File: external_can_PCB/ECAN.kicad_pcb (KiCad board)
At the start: 4 copper layers, 42.8 x 38.1 mm, 13 parts, among them J1 Conn_01x04, J2 Conn_01x06, J4 Conn_02x05_Top_Bottom, U2 SN65HVD230, U3 TXB0104D, U4 IFX27001TFV33, U5 STM32L562RETx

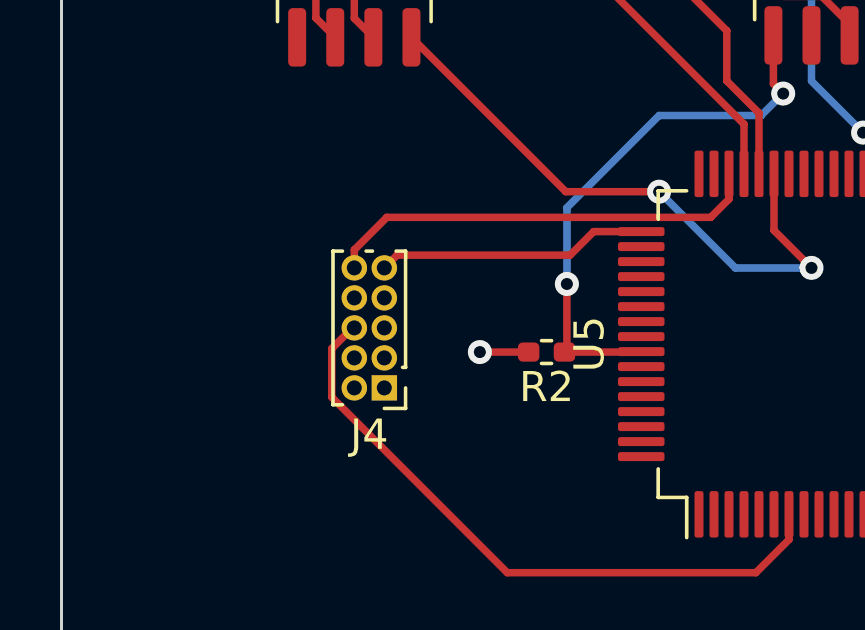
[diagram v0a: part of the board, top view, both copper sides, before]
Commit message: Added micro SD Card slot and oscillator
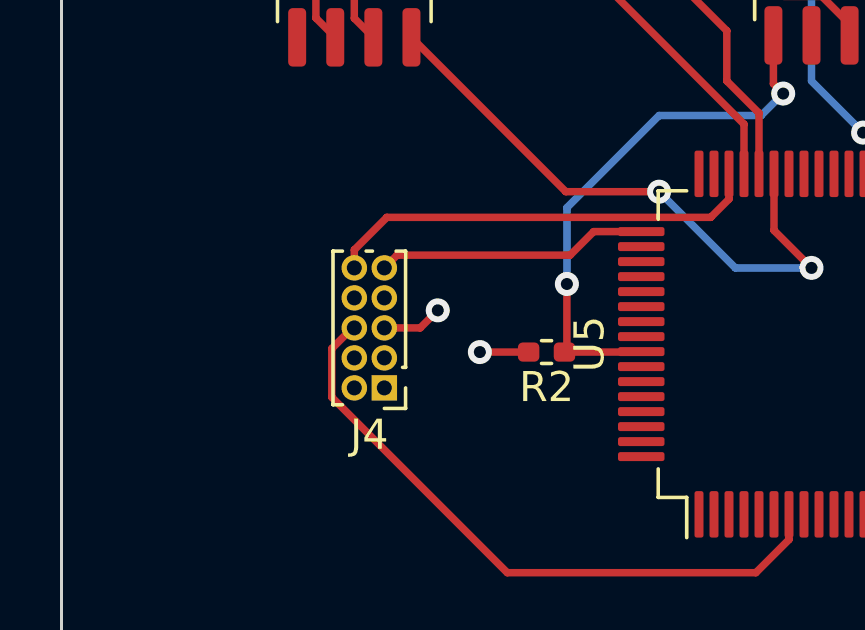
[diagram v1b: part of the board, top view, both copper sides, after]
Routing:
- net GND: track 22.5 -> 24.5 mm, vias 8 -> 9
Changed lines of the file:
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@@
   (segment (start 157.933364 78.74) (end 159.459682 80.266318) (width 0.25) (layer "F.Cu") (net 2))
   (segment (start 151.07 74.87) (end 149.86 73.66) (width 0.25) (layer "F.Cu") (net 2))
+  (segment (start 129.19754 95.98) (end 129.782471 95.395069) (width 0.25) (layer "F.Cu") (net 2))
   (segment (start 140.97 79.687518) (end 141.382865 79.274653) (width 0.25) (layer "F.Cu") (net 2))
   (segment (start 130.75 78.8024) (end 130.77949 78.83189) (width 0.25) (layer "F.Cu") (net 2))
@@
   (segment (start 153.745728 79.13812) (end 157.08188 79.13812) (width 0.25) (layer "F.Cu") (net 2))
   (segment (start 132.811255 96.785413) (end 131.185457 96.785413) (width 0.25) (layer "F.Cu") (net 2))
+  (segment (start 128 95.98) (end 129.19754 95.98) (width 0.25) (layer "F.Cu") (net 2))
   (segment (start 151.07 76.1925) (end 151.07 74.87) (width 0.25) (layer "F.Cu") (net 2))
   (segment (start 149.86 80.7125) (end 149.86 78.74) (width 0.25) (layer "F.Cu") (net 2))
@@
   (via (at 149.86 83.82) (size 0.8) (drill 0.4) (layers "F.Cu" "B.Cu") (net 2))
   (via (at 131.185457 96.785413) (size 0.8) (drill 0.4) (layers "F.Cu" "B.Cu") (net 2))
+  (via (at 129.782471 95.395069) (size 0.8) (drill 0.4) (layers "F.Cu" "B.Cu") (net 2))
   (via (at 149.86 78.74) (size 0.8) (drill 0.4) (layers "F.Cu" "B.Cu") (net 2))
   (segment (start 159.459682 81.401318) (end 158.156 82.705) (width 0.25) (layer "F.Cu") (net 3))

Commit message: PCB layout v1
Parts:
- removed J2: Conn_01x06, Connector_JST:JST_EH_S6B-EH_1x06_P2.50mm_Horizontal
- removed U4: IFX27001TFV33, Package_TO_SOT_SMD:TO-252-3_TabPin2
- added C10: 0.1 uF, Capacitor_SMD:C_0402_1005Metric_Pad0.74x0.62mm_HandSolder, B.Cu at (128.5, 75.2)
- added C11: 0.1 uF, Capacitor_SMD:C_0402_1005Metric_Pad0.74x0.62mm_HandSolder, F.Cu at (154.5, 59.3)
- added C12: 0.1 uF, Capacitor_SMD:C_0402_1005Metric_Pad0.74x0.62mm_HandSolder, F.Cu at (143.1, 75.4)
- added C13: 0.1 uF, Capacitor_SMD:C_0402_1005Metric_Pad0.74x0.62mm_HandSolder, F.Cu at (153.4, 65.5)
- added C14: 0.1 uF, Capacitor_SMD:C_0402_1005Metric_Pad0.74x0.62mm_HandSolder, F.Cu at (153.4, 61.0)
- added C15: 0.1 uF, Capacitor_SMD:C_0402_1005Metric_Pad0.74x0.62mm_HandSolder, F.Cu at (140.5, 63.3)
- added C16: 0.1 uF, Capacitor_SMD:C_0402_1005Metric_Pad0.74x0.62mm_HandSolder, F.Cu at (140.0, 48.7)
- added C17: 0.1 uF, Capacitor_SMD:C_0402_1005Metric_Pad0.74x0.62mm_HandSolder, F.Cu at (133.5, 48.7)
- added C5: 5pF, Capacitor_SMD:C_0402_1005Metric_Pad0.74x0.62mm_HandSolder, F.Cu at (126.2, 63.8)
- added C6: 5pF, Capacitor_SMD:C_0402_1005Metric_Pad0.74x0.62mm_HandSolder, F.Cu at (126.2, 52.6)
- added C7: 100nF, Capacitor_SMD:C_0402_1005Metric_Pad0.74x0.62mm_HandSolder, F.Cu at (144.2, 59.1)
- added C8: 0.1 uF, Capacitor_SMD:C_0402_1005Metric_Pad0.74x0.62mm_HandSolder, F.Cu at (148.1, 60.0)
- added C9: 0.1 uF, Capacitor_SMD:C_0402_1005Metric_Pad0.74x0.62mm_HandSolder, F.Cu at (131.6, 61.8)
- added D1: SM712_SOT23, Package_TO_SOT_SMD:SOT-23, F.Cu at (153.0, 63.3)
- added J3: JST SH 6, Connector_JST:JST_SH_BM06B-SRSS-TB_1x06-1MP_P1.00mm_Vertical, F.Cu at (137.4, 77.2)
- added J5: JST SH 6, Connector_JST:JST_SH_BM06B-SRSS-TB_1x06-1MP_P1.00mm_Vertical, F.Cu at (157.7, 52.7)
- added R3: 100k, Resistor_SMD:R_0402_1005Metric_Pad0.72x0.64mm_HandSolder, B.Cu at (140.1, 65.0)
- added R4: 100k, Resistor_SMD:R_0402_1005Metric_Pad0.72x0.64mm_HandSolder, B.Cu at (142.4, 65.0)
- added R5: 100k, Resistor_SMD:R_0402_1005Metric_Pad0.72x0.64mm_HandSolder, B.Cu at (133.5, 65.0)
- added R6: 100k, Resistor_SMD:R_0402_1005Metric_Pad0.72x0.64mm_HandSolder, B.Cu at (135.8, 65.0)
- added R7: 200k, Resistor_SMD:R_0402_1005Metric_Pad0.72x0.64mm_HandSolder, F.Cu at (128.3, 55.8)
- added R8: 100k, Resistor_SMD:R_0402_1005Metric_Pad0.72x0.64mm_HandSolder, F.Cu at (134.3, 73.9)
- added R9: 100k, Resistor_SMD:R_0402_1005Metric_Pad0.72x0.64mm_HandSolder, F.Cu at (135.3, 72.4)
- added U1: SN65HVD232, Package_SO:SOIC-8_3.9x4.9mm_P1.27mm, F.Cu at (146.6, 63.3)
- added Y1: 8 Mhz, Crystal:Crystal_SMD_0603-2Pin_6.0x3.5mm_HandSoldering, F.Cu at (125.7, 58.2)
- C1: value 100 nF -> 1 uF
- C2: value 10 uF -> 1 uF
- J1: value Conn_01x04 -> JST SH 4; footprint Connector_JST:JST_EH_S4B-EH_1x04_P2.50mm_Horizontal -> Connector_JST:JST_SH_BM04B-SRSS-TB_1x04-1MP_P1.00mm_Vertical
- J4: value Conn_02x05_Top_Bottom -> Micro_SD_Card; footprint Connector_PinHeader_1.00mm:PinHeader_2x05_P1.00mm_Vertical -> Connector_Card:microSD_HC_Wuerth_693072010801; moved to B.Cu
- U2: value SN65HVD230 -> AP2127N-3.3; footprint Package_SO:SOIC-8_3.9x4.9mm_P1.27mm -> Package_TO_SOT_SMD:SOT-223-3_TabPin2
- moved U2 45.8 mm to (150.0, 44.2), turned to 180 degrees
- moved R2 42.2 mm to (152.1, 58.9)
- moved U5 40.9 mm to (137.0, 56.0), turned to 180 degrees
- moved C2 38.9 mm to (145.0, 44.8), turned to -90 degrees
- moved C3 37.7 mm to (151.9, 48.7), turned to 0 degrees
- moved J1 37.3 mm to (157.8, 62.2), turned to -90 degrees
- moved C4 32.6 mm to (148.6, 48.7), turned to 180 degrees
- moved C1 32.1 mm to (156.8, 47.2)
- moved U3 30.4 mm to (150.1, 53.8), turned to 0 degrees
- moved R1 28.4 mm to (150.7, 63.3), turned to -90 degrees
- moved J4 25.7 mm to (137.3, 74.0), turned to 0 degrees
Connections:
- C1 pad 1: Net-(J2-Pin_6) -> Net-(J5-Pin_1)
- C3 pad 1: Net-(J2-Pin_6) -> Net-(J5-Pin_1)
- J1 pad 2: Net-(J1-Pin_2) -> GND
- J1 pad 3: Net-(J1-Pin_3) -> Net-(D1-A2)
- J1 pad 4: GND -> Net-(D1-A1)
- J4 pad 1: +3.3V -> Net-(J4-DAT2)
- J4 pad 2: unconnected-(J4-Pin_2-Pad2) -> Net-(J4-DAT3/CD)
- J4 pad 3: unconnected-(J4-Pin_3-Pad3) -> Net-(J4-CMD)
- J4 pad 4: unconnected-(J4-Pin_4-Pad4) -> +3.3V
- J4 pad 5: GND -> Net-(J4-CLK)
- J4 pad 6: Net-(J4-Pin_6) -> GND
- J4 pad 7: unconnected-(J4-Pin_7-Pad7) -> Net-(J4-DAT0)
- J4 pad 8: unconnected-(J4-Pin_8-Pad8) -> Net-(J4-DAT1)
- J4 pad 9: Net-(J4-Pin_9) -> GND
- R1 pad 1: Net-(J1-Pin_2) -> Net-(D1-A2)
- R1 pad 2: Net-(J1-Pin_3) -> Net-(D1-A1)
- U2 pad 1: Net-(U2-D) -> GND
- U2 pad 2: GND -> +3.3V
- U2 pad 3: +3.3V -> Net-(J5-Pin_1)
- U3 pad 14: Net-(J2-Pin_6) -> Net-(J5-Pin_1)
- U5 pad 1: unconnected-(U5-VBAT-Pad1) -> Net-(U5-VBAT)
- U5 pad 12: unconnected-(U5-VSSA-Pad12) -> GND
- U5 pad 13: unconnected-(U5-VDDA-Pad13) -> +3V3
- U5 pad 39: unconnected-(U5-PC8-Pad39) -> Net-(J4-DAT0)
- U5 pad 40: unconnected-(U5-PC9-Pad40) -> Net-(J4-DAT1)
- U5 pad 43: Net-(U2-Rs) -> unconnected-(U5-PA10-Pad43)
- U5 pad 44: Net-(U2-R) -> Net-(U1-R)
- U5 pad 45: Net-(U2-D) -> Net-(U1-D)
- U5 pad 46: Net-(J4-Pin_10) -> Net-(J3-Pin_4)
- U5 pad 48: unconnected-(U5-VDDUSB-Pad48) -> +3V3
- U5 pad 49: Net-(J4-Pin_9) -> Net-(J3-Pin_3)
- U5 pad 5: unconnected-(U5-PH0-Pad5) -> Net-(U5-PH0)
- U5 pad 51: unconnected-(U5-PC10-Pad51) -> Net-(J4-DAT2)
- U5 pad 52: unconnected-(U5-PC11-Pad52) -> Net-(J4-DAT3/CD)
- U5 pad 53: unconnected-(U5-PC12-Pad53) -> Net-(J4-CLK)
- U5 pad 54: unconnected-(U5-PD2-Pad54) -> Net-(J4-CMD)
- U5 pad 6: unconnected-(U5-PH1-Pad6) -> Net-(U5-PH1)
- U5 pad 60: unconnected-(U5-PH3-Pad60) -> Net-(J3-Pin_5)
- U5 pad 7: Net-(J4-Pin_6) -> Net-(J3-Pin_6)
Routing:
- net Net-(J3-Pin_6): track 0.00 -> 28.5 mm
- net Net-(J4-DAT1): track 0.00 -> 27.2 mm, vias 0 -> 1
- net Net-(U2-R): track 26.9 -> 0.00 mm, vias 2 -> 0
- net Net-(J4-DAT0): track 0.00 -> 26.5 mm, vias 0 -> 1
- net Net-(J4-Pin_6): track 21.6 -> 0.00 mm
- net Net-(J3-Pin_4): track 0.00 -> 21.3 mm, vias 0 -> 2
- net Net-(U5-PH0): track 0.00 -> 21.0 mm, vias 0 -> 2
- net Net-(U1-D): track 0.00 -> 20.6 mm, vias 0 -> 2
- net Net-(U2-Rs): track 20.2 -> 0.00 mm, vias 2 -> 0
- net Net-(J2-Pin_6): track 19.9 -> 0.00 mm
- net Net-(U1-R): track 0.00 -> 19.7 mm, vias 0 -> 2
- net GND: track 24.5 -> 44.0 mm, vias 9 -> 24
- net +3.3V: track 18.4 -> 36.0 mm, vias 2 -> 5
- net Net-(J3-Pin_3): track 0.00 -> 16.8 mm, vias 0 -> 2
- net Net-(U2-D): track 16.0 -> 0.00 mm
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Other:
- board outline removed

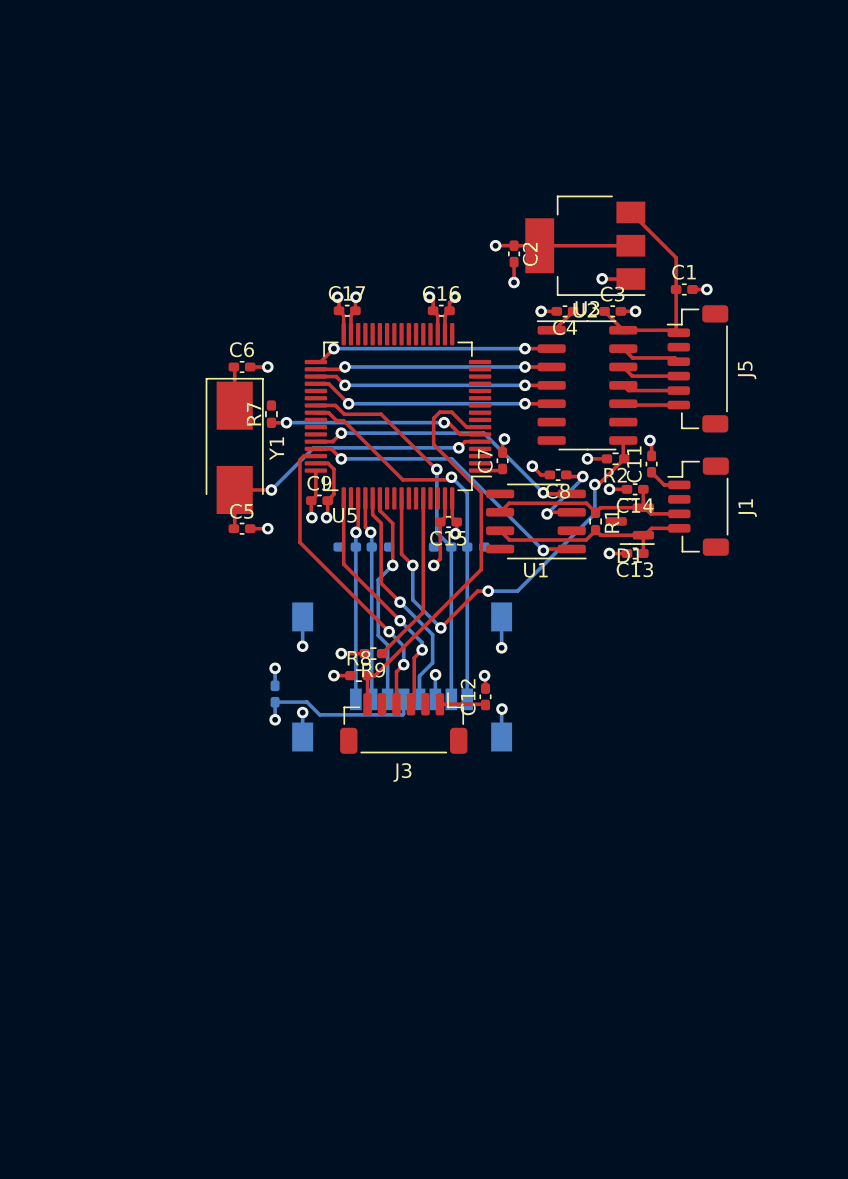
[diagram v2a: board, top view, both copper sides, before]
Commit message: Redid ECAN Design: - Removed SPI Level Shifter * Changed JST SH Connector to JST GH * Cleaned up schematic
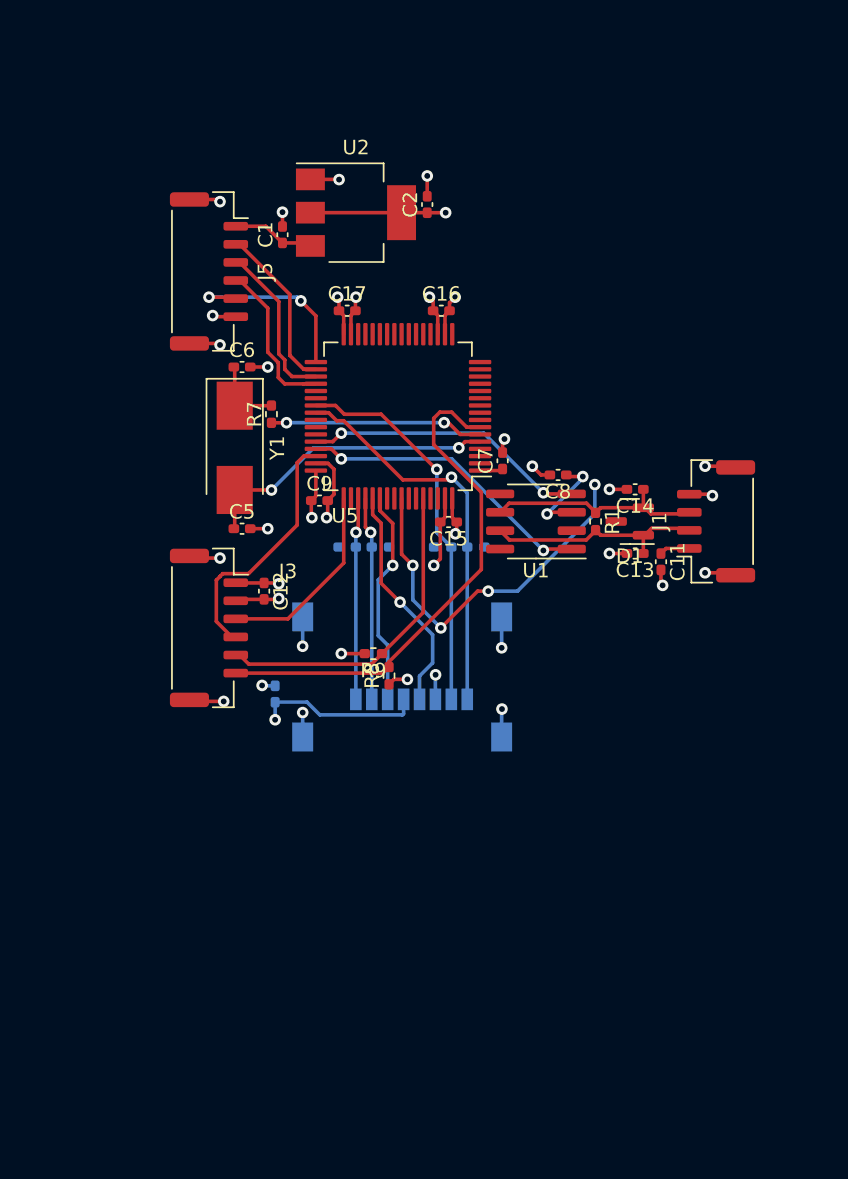
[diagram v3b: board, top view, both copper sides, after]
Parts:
- removed C3, C4: 0.1 uF, Capacitor_SMD:C_0402_1005Metric_Pad0.74x0.62mm_HandSolder
- removed R2: 55 kOhm, Resistor_SMD:R_0402_1005Metric_Pad0.72x0.64mm_HandSolder
- removed U3: TXB0104D, Package_SO:SOIC-14_3.9x8.7mm_P1.27mm
- J1: value JST SH 4 -> JST GH 4; footprint Connector_JST:JST_SH_BM04B-SRSS-TB_1x04-1MP_P1.00mm_Vertical -> Connector_JST:JST_GH_SM04B-GHS-TB_1x04-1MP_P1.25mm_Horizontal
- J3, J5: value JST SH 6 -> JST GH 6; footprint Connector_JST:JST_SH_BM06B-SRSS-TB_1x06-1MP_P1.00mm_Vertical -> Connector_JST:JST_GH_SM06B-GHS-TB_1x06-1MP_P1.25mm_Horizontal
- moved J5 34.5 mm to (124.0, 46.0)
- moved C1 28.0 mm to (129.0, 43.4), turned to 90 degrees
- moved C12 17.0 mm to (127.8, 68.1), turned to -90 degrees
- moved U2 16.0 mm to (134.1, 41.9), turned to 0 degrees
- moved J3 15.0 mm to (124.0, 70.6), turned to -90 degrees
- moved C2 6.90 mm to (139.0, 41.3), turned to 90 degrees
- moved C11 6.78 mm to (155.2, 66.0), turned to -90 degrees
- moved R8 2.08 mm to (136.4, 73.9), turned to 90 degrees
- moved J1 1.59 mm to (159.0, 63.2), turned to 90 degrees
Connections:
- net Net-(J3-Pin_3) renamed /JTCK/SWCLK
- net Net-(J3-Pin_4) renamed /JTMS/SWDIO
- net Net-(J3-Pin_5) renamed /BOOT0
- net Net-(J3-Pin_6) renamed /NRST
- net Net-(U1-D) renamed /FDCAN1_TX
- net Net-(U1-R) renamed /FDCAN1_RX
- C15 pad 1: +3V3 -> +3.3V
- C16 pad 1: +3V3 -> +3.3V
- C17 pad 1: +3V3 -> +3.3V
- C7 pad 2: +3V3 -> +3.3V
- C9 pad 1: +3V3 -> +3.3V
- J1 pad 2: GND -> Net-(D1-A1)
- J1 pad 4: Net-(D1-A1) -> GND
- J5 pad 2: GND -> /SPI2_SCK_3.3V
- J5 pad 3: Net-(J5-Pin_3) -> /SPI3_MISO_3.3V
- J5 pad 4: Net-(J5-Pin_4) -> /SPI2_MOSI_3.3V
- J5 pad 5: Net-(J5-Pin_5) -> /SPI2_NSS_3.3V
- J5 pad 6: Net-(J5-Pin_6) -> GND
- U5 pad 13: +3V3 -> +3.3V
- U5 pad 19: +3V3 -> +3.3V
- U5 pad 32: +3V3 -> +3.3V
- U5 pad 33: Net-(U3-A1) -> /SPI2_NSS_3.3V
- U5 pad 34: Net-(U3-A2) -> /SPI2_SCK_3.3V
- U5 pad 35: Net-(U3-A3) -> /SPI3_MISO_3.3V
- U5 pad 36: Net-(U3-A4) -> /SPI2_MOSI_3.3V
- U5 pad 48: +3V3 -> +3.3V
- U5 pad 57: Net-(U3-OE) -> unconnected-(U5-PB5-Pad57)
- U5 pad 64: +3V3 -> +3.3V
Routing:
- net Net-(U3-OE): track 30.1 -> 0.00 mm, vias 4 -> 0
- net unconnected-(U5-PB5-Pad57): track 0.00 -> 26.3 mm, vias 0 -> 4
- net Net-(U3-A4): track 16.9 -> 0.00 mm, vias 2 -> 0
- net Net-(U3-A1): track 16.7 -> 0.00 mm, vias 2 -> 0
- net Net-(U3-A3): track 16.6 -> 0.00 mm, vias 2 -> 0
- net Net-(U3-A2): track 16.4 -> 0.00 mm, vias 2 -> 0
- net GND: track 44.0 -> 58.8 mm, vias 24 -> 29
- net /SPI2_NSS_3.3V: track 0.00 -> 13.0 mm, vias 0 -> 2
- net +3V3: track 12.5 -> 0.00 mm, vias 5 -> 0
- net /SPI2_SCK_3.3V: track 0.00 -> 11.6 mm
- net /SPI3_MISO_3.3V: track 0.00 -> 11.3 mm
- net /SPI2_MOSI_3.3V: track 0.00 -> 10.9 mm
- net /BOOT0: track 11.9 -> 22.6 mm
- net +3.3V: track 36.0 -> 46.5 mm, vias 5 -> 11
- net Net-(J5-Pin_1): track 15.4 -> 5.72 mm
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
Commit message: Added screw holes and layer pours
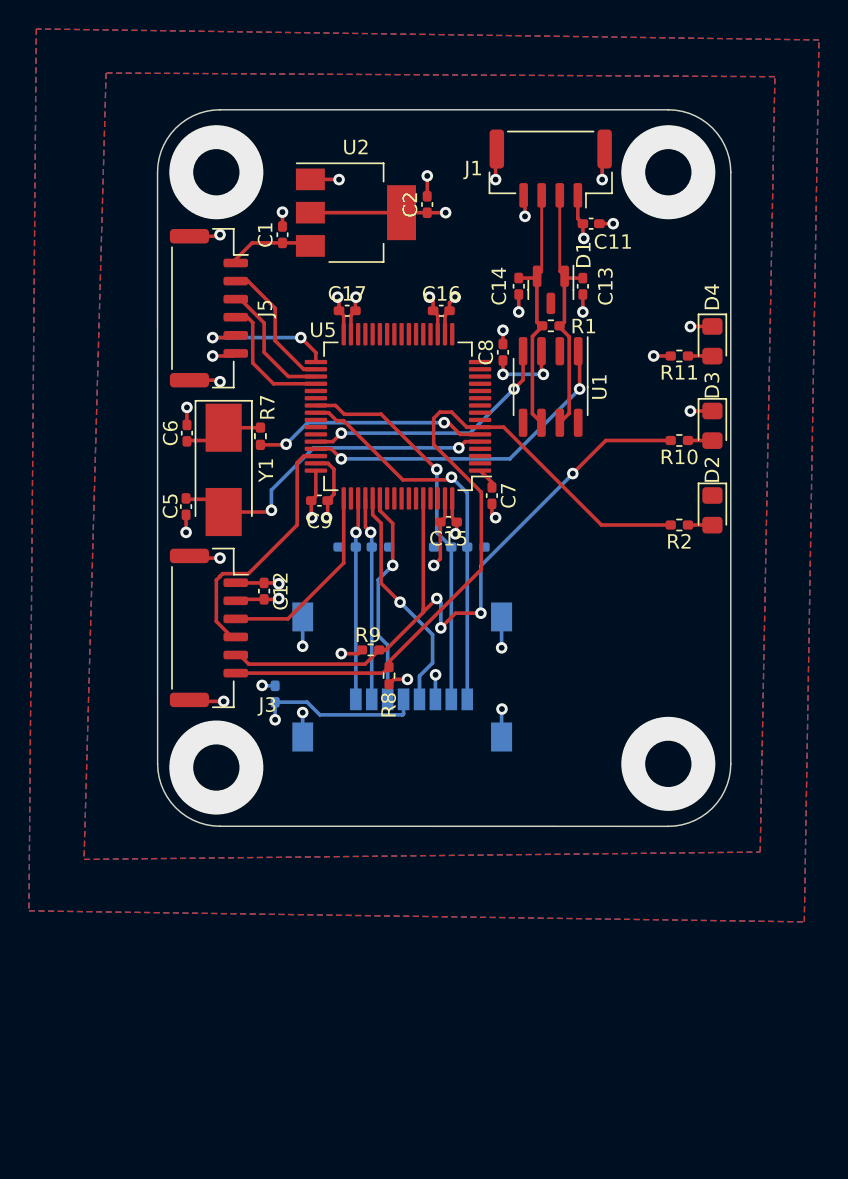
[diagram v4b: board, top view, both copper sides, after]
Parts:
- added D2: LED, LED_SMD:LED_0805_2012Metric_Pad1.15x1.40mm_HandSolder, F.Cu at (158.8, 62.5)
- added D3: LED, LED_SMD:LED_0805_2012Metric_Pad1.15x1.40mm_HandSolder, F.Cu at (158.8, 56.6)
- added D4: LED, LED_SMD:LED_0805_2012Metric_Pad1.15x1.40mm_HandSolder, F.Cu at (158.8, 50.8)
- added R10: 220, Resistor_SMD:R_0402_1005Metric_Pad0.72x0.64mm_HandSolder, F.Cu at (156.5, 57.7)
- added R11: 220, Resistor_SMD:R_0402_1005Metric_Pad0.72x0.64mm_HandSolder, F.Cu at (156.5, 51.8)
- added R2: 200, Resistor_SMD:R_0402_1005Metric_Pad0.72x0.64mm_HandSolder, F.Cu at (156.5, 63.5)
- moved J1 26.9 mm to (147.6, 38.9), turned to 180 degrees
- moved C11 23.9 mm to (150.4, 42.7), turned to 0 degrees
- moved C13 18.8 mm to (149.8, 47.0), turned to -90 degrees
- moved D1 16.9 mm to (147.6, 47.2), turned to -90 degrees
- moved C14 16.2 mm to (145.4, 47.0), turned to -90 degrees
- moved R1 13.9 mm to (147.6, 49.7), turned to 0 degrees
- moved U1 9.35 mm to (147.6, 54.0), turned to -90 degrees
- moved C8 9.29 mm to (144.3, 51.6), turned to 90 degrees
- moved C6 5.95 mm to (122.4, 57.1), turned to 90 degrees
- moved C5 4.16 mm to (122.4, 62.2), turned to -90 degrees
- moved J5 2.54 mm to (124.0, 48.5)
- moved C7 2.52 mm to (143.5, 61.5), turned to -90 degrees
- moved R7 1.70 mm to (127.5, 57.4)
- moved Y1 1.70 mm to (125.0, 59.7)
- moved R9 0.32 mm to (135.1, 72.1)
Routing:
- net /BOOT0: track 22.6 -> 49.3 mm, vias 0 -> 4
- net unconnected-(U5-PB5-Pad57): track 26.3 -> 0.00 mm, vias 4 -> 0
- net /NRST: track 35.6 -> 51.6 mm
- net Net-(D1-A2): track 14.5 -> 17.7 mm
- net Net-(D1-A1): track 14.6 -> 17.8 mm
- net /SPI2_NSS_3.3V: track 13.0 -> 9.88 mm
- net /FDCAN1_TX: track 20.6 -> 23.2 mm
- net /SPI3_MISO_3.3V: track 11.3 -> 8.94 mm
- net Net-(U5-PH0): track 21.0 -> 23.3 mm
- net /SPI2_SCK_3.3V: track 11.6 -> 9.38 mm
- net GND: track 58.8 -> 60.9 mm, vias 29 -> 31
- net /SPI2_MOSI_3.3V: track 10.9 -> 9.08 mm
- net Net-(D4-A): track 0.00 -> 1.69 mm
- net Net-(D3-A): track 0.00 -> 1.69 mm
- net Net-(D2-A): track 0.00 -> 1.69 mm
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- added copper zone on In2.Cu, net +3.3V
- added copper zone on B.Cu, net /BOOT0
- added copper zone on F.Cu, net /BOOT0
- added copper zone on B.Cu, net /FDCAN1_RX
- added copper zone on F.Cu, net /FDCAN1_RX
- added copper zone on In1.Cu, net GND
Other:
- board outline added: 39.6 x 49.5 mm
